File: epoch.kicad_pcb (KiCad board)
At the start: 4 copper layers, 28 x 34 mm, 33 parts, among them J1 USB_OTG, J2 CONN_01X05, J3 CONN_01X05, P3 CONN_01X10, SW1 SW_Reset, U1 MIC5219-3.3BM5, U2 ATSAMD21Ennc-AU, U3 DS3231MZ, U4 MCP7940N-I/SN, U5 74HC1G14GW, U6 MH2mm, U7 MH2mm, U8 MH2mm, U9 MH2mm

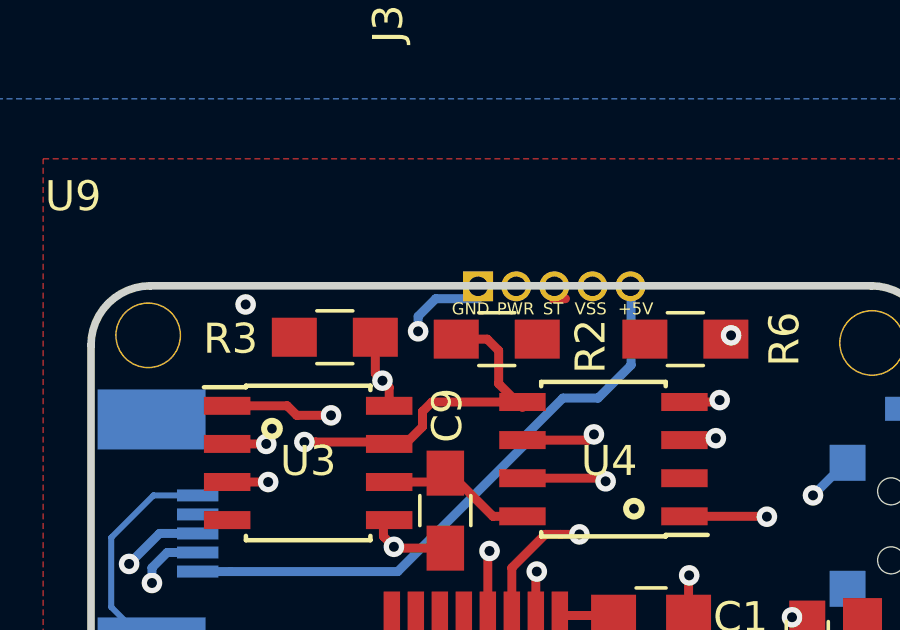
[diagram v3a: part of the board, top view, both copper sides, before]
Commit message: Fix ground plane
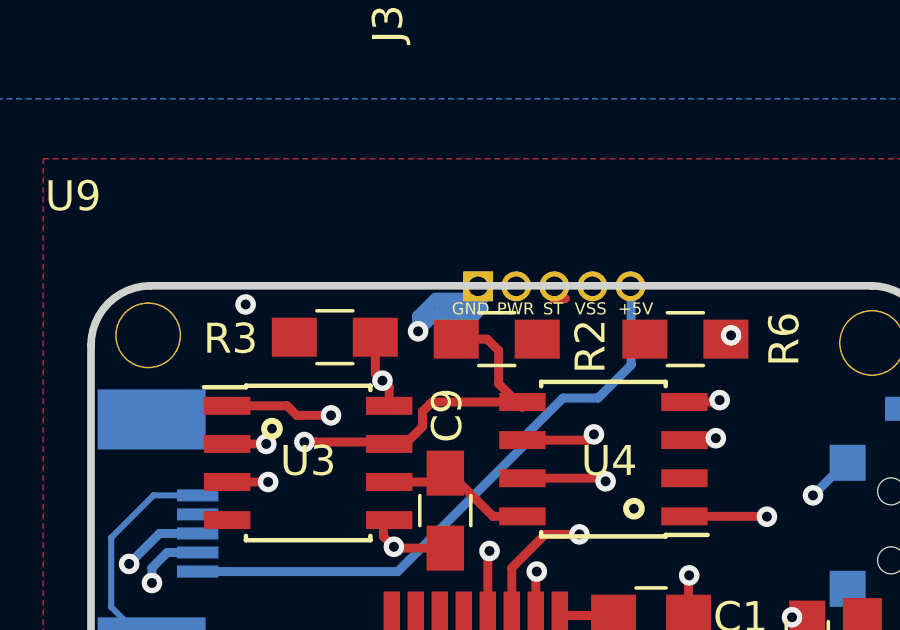
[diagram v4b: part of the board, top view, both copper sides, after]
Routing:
- net (GND): track 37.6 -> 42.8 mm
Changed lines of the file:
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@@
     (thickness 1.6002)
     (drawings 27)
-    (tracks 472)
+    (tracks 478)
     (zones 0)
     (modules 33)
@@
   )
   (setup
-    (last_trace_width 0.3)
+    (last_trace_width 0.4)
     (user_trace_width 0.1524)
     (user_trace_width 0.2)
@@
     (user_trace_width 0.4)
     (trace_clearance 0.1524)
-    (zone_clearance 0.508)
+    (zone_clearance 0)
     (zone_45_only no)
     (trace_min 0.1524)
@@
     (visible_elements 7FFFFFBF)
     (pcbplotparams
-      (layerselection 0x010f0_80000007)
+      (layerselection 0x010f0_ffffffff)
       (usegerberextensions true)
       (usegerberattributes false)
@@
       (drillshape 0)
       (scaleselection 1)
-      (outputdirectory ""))
+      (outputdirectory "plot/"))
   )
   (net 0 "")
@@
     (add_net VDD)
   )
+  (module my-fp-library:Pin_Header_Straight_1x05_Pitch1.27mm_no_silk (layer F.Cu)
+    (at 114.25 54.5 90)
+    (descr "Through hole straight pin header, 1x05, 1.27mm pitch, single row")
+    (tags "Through hole pin header THT 1x05 1.27mm single row")
+    (fp_text reference J3 (at 8.75 -3 90) (layer F.SilkS)
+      (effects (font (size 1 1) (thickness 0.15)))
+    )
+    (fp_text value CONN_01X05 (at 6.275 25.1 90) (layer F.Fab)
+      (effects (font (size 1 1) (thickness 0.15)))
+    )
+    (fp_line (start 1.6 -0.9) (end -1.6 -0.9) (layer F.CrtYd) (width 0.05))
+    (fp_line (start 1.6 6) (end 1.6 -0.9) (layer F.CrtYd) (width 0.05))
+    (fp_line (start -1.6 6) (end 1.6 6) (layer F.CrtYd) (width 0.05))
+    (fp_line (start -1.6 -0.9) (end -1.6 6) (layer F.CrtYd) (width 0.05))
+    (fp_line (start 1.27 -0.635) (end -1.27 -0.635) (layer F.Fab) (width 0.1))
+    (fp_line (start 1.27 5.715) (end 1.27 -0.635) (layer F.Fab) (width 0.1))
+    (fp_line (start -1.27 5.715) (end 1.27 5.715) (layer F.Fab) (width 0.1))
+    (fp_line (start -1.27 -0.635) (end -1.27 5.715) (layer F.Fab) (width 0.1))
+    (pad 5 thru_hole oval (at 0 5.08 90) (size 1 1) (drill 0.65) (layers *.Cu *.Mask)
+      (net 29 VDD))
+    (pad 4 thru_hole oval (at 0 3.81 90) (size 1 1) (drill 0.65) (layers *.Cu *.Mask)
+      (net 26 "(+5)"))
+    (pad 3 thru_hole oval (at 0 2.54 90) (size 1 1) (drill 0.65) (layers *.Cu *.Mask)
+      (net 28 STAT))
+    (pad 2 thru_hole oval (at 0 1.27 90) (size 1 1) (drill 0.65) (layers *.Cu *.Mask)
+      (net 27 PWR_SENSE))
+    (pad 1 thru_hole rect (at 0 0 90) (size 1 1) (drill 0.65) (layers *.Cu *.Mask)
+      (net 2 "(GND)"))
+    (model Pin_Headers.3dshapes/Pin_Header_Straight_1x05_Pitch1.27mm.wrl
+      (at (xyz 0 0 0))
+      (scale (xyz 1 1 1))
+      (rotate (xyz 0 0 0))
+    )
+  )
   (module TO_SOT_Packages_SMD:SOT-23-5 (layer F.Cu)
     (at 104.7115 76.5175)
@@
     (pad 1 thru_hole circle (at 0 0) (size 2.2 2.2) (drill 2.1) (layers *.Cu *.Mask))
   )
-  (module my-fp-library:Pin_Header_Straight_1x05_Pitch1.27mm_no_silk (layer F.Cu)
-    (at 114.25 54.5 90)
-    (descr "Through hole straight pin header, 1x05, 1.27mm pitch, single row")
-    (tags "Through hole pin header THT 1x05 1.27mm single row")
-    (fp_text reference J3 (at 8.75 -3 90) (layer F.SilkS)
-      (effects (font (size 1 1) (thickness 0.15)))
-    )
-    (fp_text value CONN_01X05 (at 6.275 25.1 90) (layer F.Fab)
-      (effects (font (size 1 1) (thickness 0.15)))
-    )
-    (fp_line (start 1.6 -0.9) (end -1.6 -0.9) (layer F.CrtYd) (width 0.05))
-    (fp_line (start 1.6 6) (end 1.6 -0.9) (layer F.CrtYd) (width 0.05))
-    (fp_line (start -1.6 6) (end 1.6 6) (layer F.CrtYd) (width 0.05))
-    (fp_line (start -1.6 -0.9) (end -1.6 6) (layer F.CrtYd) (width 0.05))
-    (fp_line (start 1.27 -0.635) (end -1.27 -0.635) (layer F.Fab) (width 0.1))
-    (fp_line (start 1.27 5.715) (end 1.27 -0.635) (layer F.Fab) (width 0.1))
-    (fp_line (start -1.27 5.715) (end 1.27 5.715) (layer F.Fab) (width 0.1))
-    (fp_line (start -1.27 -0.635) (end -1.27 5.715) (layer F.Fab) (width 0.1))
-    (pad 5 thru_hole oval (at 0 5.08 90) (size 1 1) (drill 0.65) (layers *.Cu *.Mask)
-      (net 29 VDD))
-    (pad 4 thru_hole oval (at 0 3.81 90) (size 1 1) (drill 0.65) (layers *.Cu *.Mask)
-      (net 26 "(+5)"))
-    (pad 3 thru_hole oval (at 0 2.54 90) (size 1 1) (drill 0.65) (layers *.Cu *.Mask)
-      (net 28 STAT))
-    (pad 2 thru_hole oval (at 0 1.27 90) (size 1 1) (drill 0.65) (layers *.Cu *.Mask)
-      (net 27 PWR_SENSE))
-    (pad 1 thru_hole rect (at 0 0 90) (size 1 1) (drill 0.65) (layers *.Cu *.Mask)
-      (net 2 "(GND)"))
-    (model Pin_Headers.3dshapes/Pin_Header_Straight_1x05_Pitch1.27mm.wrl
-      (at (xyz 0 0 0))
-      (scale (xyz 1 1 1))
-      (rotate (xyz 0 0 0))
-    )
+  (gr_text GND (at 114 55.25) (layer F.SilkS)
+    (effects (font (size 0.4 0.4) (thickness 0.1)))
   )
   (gr_text PWR (at 115.5 55.25) (layer F.SilkS)
@@
   )
   (gr_text +5V (at 119.5 55.25) (layer F.SilkS)
-    (effects (font (size 0.4 0.4) (thickness 0.1)))
-  )
-  (gr_text GND (at 114 55.25) (layer F.SilkS)
     (effects (font (size 0.4 0.4) (thickness 0.1)))
   )
@@
   (segment (start 103.4288 61.468) (end 104.9528 61.468) (width 0.2) (layer B.Cu) (net 2) (status 20))
   (via (at 112.25 56) (size 0.6858) (drill 0.3302) (layers F.Cu B.Cu) (net 2))
-  (segment (start 112.25 55.5) (end 112.83759 54.91241) (width 0.3) (layer B.Cu) (net 2))
-  (segment (start 112.83759 54.91241) (end 114.25 54.91241) (width 0.3) (layer B.Cu) (net 2))
-  (segment (start 112.25 55.5) (end 112.25 56) (width 0.3) (layer B.Cu) (net 2))
+  (segment (start 112.25 55.5) (end 112.83759 54.91241) (width 0.4) (layer B.Cu) (net 2))
+  (segment (start 112.83759 54.91241) (end 114.25 54.91241) (width 0.4) (layer B.Cu) (net 2))
+  (segment (start 112.25 55.5) (end 112.25 56) (width 0.4) (layer B.Cu) (net 2))
+  (segment (start 113.28759 54.96241) (end 114.375 54.96241) (width 0.4) (layer B.Cu) (net 2))
+  (segment (start 113.025 55.225) (end 113.28759 54.96241) (width 0.4) (layer B.Cu) (net 2))
+  (segment (start 114.375 55.225) (end 113.025 55.225) (width 0.4) (layer B.Cu) (net 2))
+  (segment (start 114.15 55.45) (end 114.375 55.225) (width 0.4) (layer B.Cu) (net 2))
+  (segment (start 112.8 55.45) (end 114.15 55.45) (width 0.4) (layer B.Cu) (net 2))
+  (segment (start 112.25 56) (end 112.8 55.45) (width 0.4) (layer B.Cu) (net 2))
   (segment (start 114.573 73.973) (end 114.573 75.292) (width 0.3) (layer F.Cu) (net 3) (status 10))
   (segment (start 114.32 75.545) (end 114.32 77.1525) (width 0.3) (layer F.Cu) (net 3) (status 20))
@@
   (segment (start 117.007101 56.842899) (end 118.05 55.8) (width 0.3) (layer In2.Cu) (net 26))
   (segment (start 118.05 55.8) (end 118.05 54.91241) (width 0.3) (layer In2.Cu) (net 26))
-  (segment (start 104.902 64.008) (end 105.992 64.008) (width 0.3) (layer B.Cu) (net 29))
   (segment (start 118.423 66.923) (end 117.323 66.923) (width 0.3) (layer F.Cu) (net 27))
   (via (at 117.323 66.923) (size 0.6858) (drill 0.3302) (layers F.Cu B.Cu) (net 27))
@@
   (segment (start 117.625401 60.875645) (end 118.755301 59.745745) (width 0.3) (layer In1.Cu) (net 28))
   (segment (start 116.91241 54.91241) (end 116.75 54.91241) (width 0.3) (layer In1.Cu) (net 28))
+  (segment (start 104.902 64.008) (end 105.992 64.008) (width 0.3) (layer B.Cu) (net 29))
   (segment (start 111.572046 64.008) (end 115.8 59.780046) (width 0.3) (layer B.Cu) (net 29))
   (segment (start 105.992 64.008) (end 111.572046 64.008) (width 0.3) (layer B.Cu) (net 29))

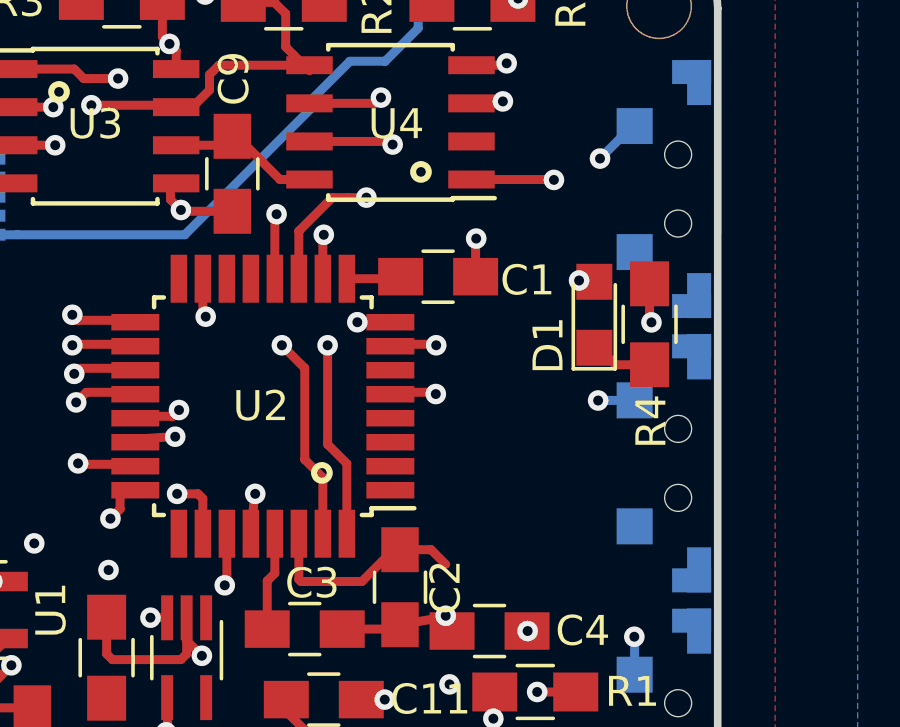
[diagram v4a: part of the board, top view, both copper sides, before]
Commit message: Update for voltage divider to get battery level
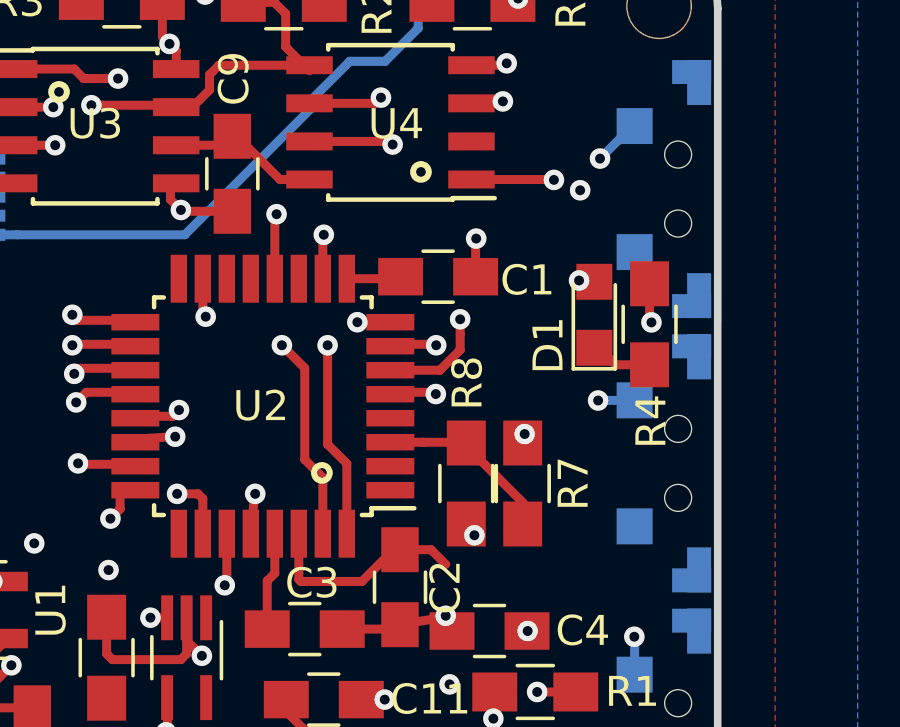
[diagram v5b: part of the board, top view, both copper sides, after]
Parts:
- added R7: 10K, Resistors_SMD:R_0805_HandSoldering, F.Cu at (122.8, 72.3)
- added R8: 10K, Resistors_SMD:R_0805_HandSoldering, F.Cu at (121.0, 72.3)
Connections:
- U2 pad 11: STAT -> (no net)
- U2 pad 3: (no net) -> BATT_VOLT
- U2 pad 6: (no net) -> STAT
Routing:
- net (+5): track 40.2 -> 60.7 mm, vias 2 -> 4
- net BATT_VOLT: track 0.00 -> 6.17 mm
- net STAT: track 14.0 -> 17.7 mm
- net (GND): track 42.8 -> 43.3 mm, vias 15 -> 16
